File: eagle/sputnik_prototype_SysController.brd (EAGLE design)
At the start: 100 x 80 mm, 64 parts, among them U1 MEGA128-A

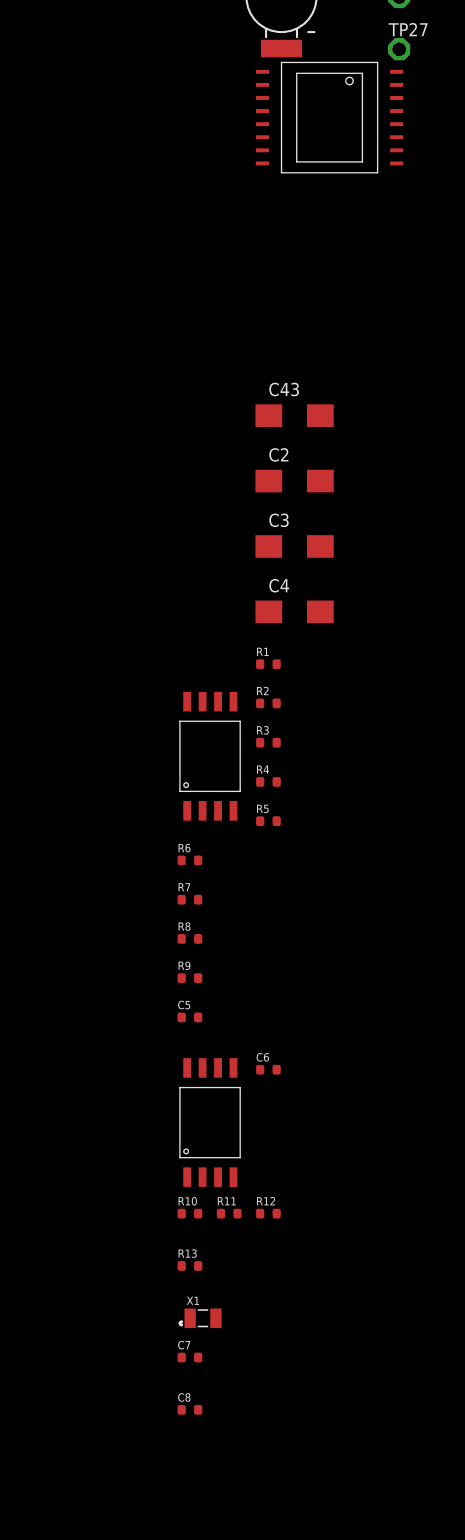
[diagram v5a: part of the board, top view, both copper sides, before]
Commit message: Got rid of SysCon LDO, fixed Optoisolator symbol
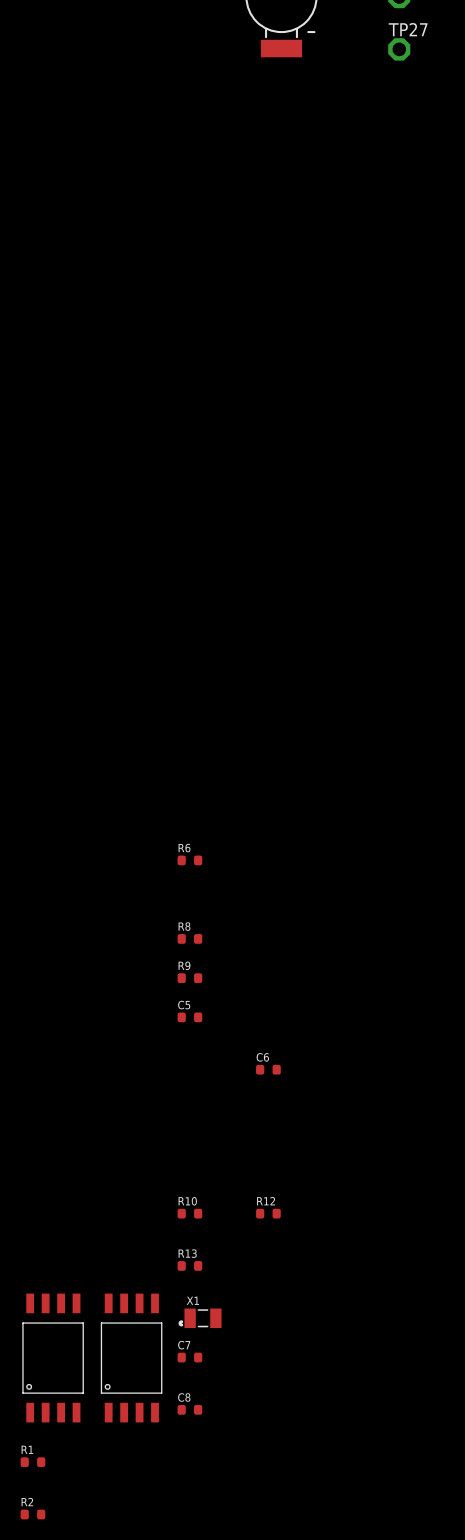
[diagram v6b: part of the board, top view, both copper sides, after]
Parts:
- removed C2, C3, C4, C43: (no value), rcl:CT6032
- removed R11, R7: 390, rcl_custom:.0603-B-NOSILK
- removed R3, R4, R5: (no value), rcl_custom:.0603-B-NOSILK
- removed U$3: ACPL-064L/K64L, psas_c3_team05:ACPL-064L/K64L
- R1, R2: value (none) -> 390
- U$1: value TPS7H1201-HT -> ACPL-064L/K64L; device psas_c3_team05:TPS7H1201-HT -> psas_c3_team05:ACPL-064L/K64L
- moved U$1 120.7 mm to (-85.1, -348.0)
- moved R2 82.0 mm to (-91.4, -369.6)
- moved R1 80.8 mm to (-91.4, -364.5)
- moved U$2 60.4 mm to (-92.7, -348.0)
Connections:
- removed net N$16: R9.2, U1.27
- removed net N$27: R11.1, U$3.2
- removed net N$5: C4.+, U$1.15
- removed net N$6: R3.2, R4.1
- removed net N$7: R5.1, U$1.9
- removed net N$8: R2.2, U$1.7
- removed net N$9: R1.1, U$1.10
- removed net UART0_TX: U$3.6
- new net N$36: C1.+
- net GND: now also R13.2, R9.2, U$1.5; no longer C2.-, C3.-, C43.-, R11.2, R2.1, R3.1, R7.2, U$1.8, U$3.5
- net N$1: no longer C4.-, R4.2, R5.2, U$1.11, U$1.12, U$1.13, U$1.14
- net N$19: now also U$2.6, U1.27; no longer R7.1, U$2.2
- net N$2: now also R1.1; no longer C43.+, U$1.1
- net N$20: now also U$2.2; no longer U$2.3
- net N$21: now also U$2.3; no longer U$2.4
- net N$26: now also U$1.1; no longer U$3.1
- net N$28: now also U$1.2; no longer U$3.3
- net N$29: now also U$1.3; no longer U$3.4
- net N$3: now also JP5.1, R2.1, TP4.TP; no longer C1.+, C2.+, R1.2, U$1.3, U$1.4, U$1.5, U$1.6
- net N$4: now also U$1.4; no longer C3.+, U$1.16
- net PTA2: now also U$1.6; no longer R13.2
- net UART0_RX: now also R1.2, U$1.7; no longer U$3.7
- net UART1_RX: now also R2.2, U$2.7; no longer JP5.1, TP4.TP, U$2.6
- net UART1_TX: now also U$2.4; no longer U$2.7
- net V+: now also U$1.8; no longer U$3.8

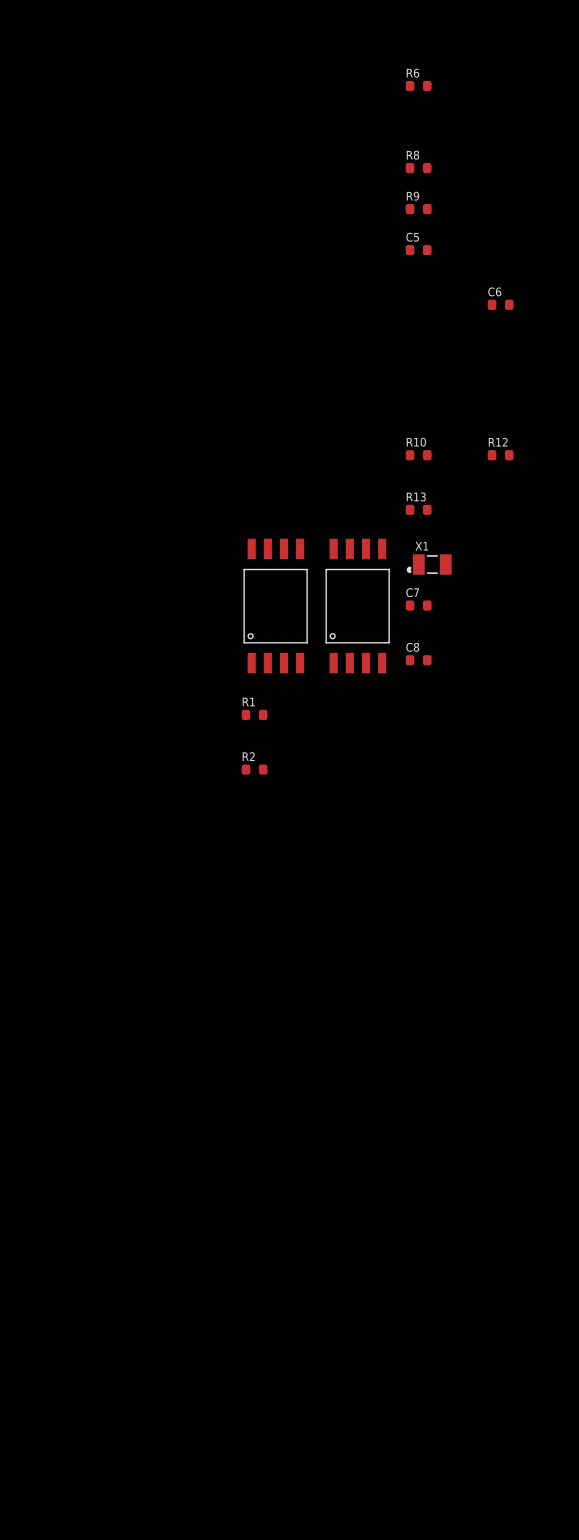
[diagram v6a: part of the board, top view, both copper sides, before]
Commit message: Fixed OIs, fixed SysCon LDO, replaced SPI cache
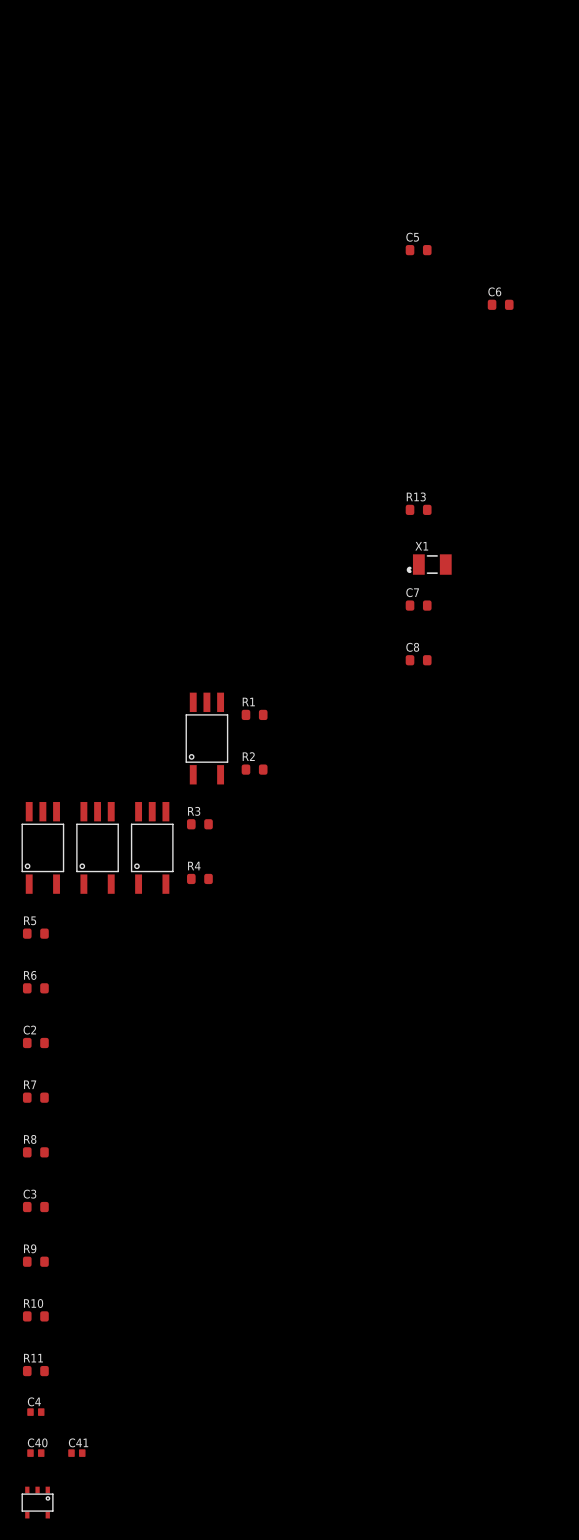
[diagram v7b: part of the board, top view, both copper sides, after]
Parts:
- removed R12: 390, rcl_custom:.0603-B-NOSILK
- added C2, C3: 0.1uF, rcl_custom:.0603-B-NOSILK
- added C4: 2.2uF, rcl_custom:.0402-B-NOSILK
- added C40: 10nF, rcl_custom:.0402-B-NOSILK
- added C41: 1uF, rcl_custom:.0402-B-NOSILK
- added R11, R3, R4, R5, R7: 390, rcl_custom:.0603-B-NOSILK
- added U$3, U$4: ACPL-M61L, psas_c3_team05:ACPL-M61L
- added U$8: AAT3215, psas_c3_team05:AAT3215
- U$1, U$2: value ACPL-064L/K64L -> ACPL-M61L; device psas_c3_team05:ACPL-064L/K64L -> psas_c3_team05:ACPL-M61L
- moved R9 104.1 mm to (-111.8, -415.3)
- moved R8 98.1 mm to (-111.8, -405.1)
- moved R6 91.1 mm to (-111.8, -389.9)
- moved R10 87.6 mm to (-111.8, -420.4)
- moved U$2 28.5 mm to (-102.9, -374.6)
- moved U$1 20.8 mm to (-97.8, -364.5)
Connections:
- net N$2 renamed PTA1/UART0_RX
- removed net N$1: C36.2, C37.2, C38.2, C39.2, JP3.4, JP3.7, U1.21, U1.52, U1.62, U1.64
- removed net N$26: R10.1, U$1.1
- removed net N$28: R12.1, U$1.2
- removed net N$29: R13.1, U$1.3
- removed net UART0_RX: R1.2, U$1.7
- new net N$16: R1.2, U$3.4
- new net N$2: C36.2, C37.2, C38.2, C39.2, C4.1, JP3.4, JP3.7, U$8.5, U1.21, U1.52, U1.62, U1.64
- new net N$23: C40.1, U$8.4
- new net N$24: R11.1, U$2.4
- new net N$5: R2.2, U$1.4
- new net N$6: R3.1, U$1.1
- new net N$7: R4.1, U$1.2
- new net N$8: R5.2, U$2.1
- new net N$9: R6.1
- new net PTA2/UART1_TX: R10.1
- net GND: now also C2.1, C3.1, C4.2, C40.2, C41.2, R4.2, R6.2, U$1.3, U$2.3, U$3.3, U$4.3, U$8.2; no longer R12.2, R8.2, U$1.5, U$2.5
- net N$10: now also R3.2; no longer R6.2
- net N$18: now also R8.1, U$4.4; no longer R6.1, U$2.1
- net N$19: now also R11.2; no longer U$2.6
- net N$20: now also R10.2, U$4.1; no longer R8.1, U$2.2
- net N$21: now also U$4.2; no longer U$2.3
- net N$3: now also R13.1, U$3.2; no longer JP5.1, R2.1, TP4.TP
- net N$36: now also C41.1, U$8.1
- net N$4: now also R7.1, U$3.1; no longer U$1.4
- net PTA1: now also R7.2; no longer R10.2
- net PTA2: now also R8.2; no longer U$1.6
- net UART1_RX: now also JP5.1, R2.1, TP4.TP; no longer R2.2, U$2.7
- net UART1_TX: now also R5.1; no longer U$2.4
- net V+: now also C2.2, C3.2, U$1.5, U$2.5, U$3.5, U$4.5; no longer U$1.8, U$2.8

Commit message: added headers to power supply
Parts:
- added D1, D2: SMD-DIODE-SCHOTTKY-40V-5A(DO-214AB)-SSC53L, SMD-DIODE-SCHOTTKY-40V-5A_DO-214AB_ SSC53L:DO-214AB
- added JP4, JP9: (no value), psas_c3_team05:1X02
- X1: value (none) -> CRYSTAL-ABRACON-ABM3-SMD; device monitor-v2:CRYSTAL-3.2X1.5-A -> crystal-abracon-abm3-smd:CRYSTAL-ABRACON-ABM3-SMD
- moved U$8 519.3 mm to (-33.0, 76.2)
- moved C40 515.5 mm to (-24.1, 74.9)
- moved C41 514.3 mm to (-27.9, 74.9)
- moved C4 512.4 mm to (-20.3, 74.9)
- moved R11 498.3 mm to (-69.8, 71.1)
- moved R10 493.6 mm to (-66.0, 71.1)
- moved R9 488.9 mm to (-62.2, 71.1)
- moved R8 479.2 mm to (-58.4, 71.1)
- moved C3 478.3 mm to (-67.3, 66.0)
- moved R7 474.6 mm to (-54.6, 71.1)
- moved R6 465.0 mm to (-50.8, 71.1)
- moved C2 463.7 mm to (-62.2, 66.0)
- moved R5 460.5 mm to (-47.0, 71.1)
- moved R4 454.0 mm to (-43.2, 71.1)
- moved R3 449.4 mm to (-39.4, 71.1)
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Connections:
- removed net N$22: C8.2, U1.24, X1.2
- new net N$1: C8.2, U1.24, X1.P$2
- new net N$25: D1.1, JP4.1
- new net N$26: D2.1, JP9.1
- net GND: now also JP4.2, JP9.2
- net N$17: now also X1.P$1; no longer X1.1
- net V+: now also D1.2, D2.2
